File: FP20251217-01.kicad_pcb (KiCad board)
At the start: 2 copper layers, 1 part, among them J1 216-3340-00-0602J

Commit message: Roughing out PCB
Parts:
- added A1: Arduino_UNO_R2, Module:Arduino_UNO_R2, F.Cu at (150.0, 100.0)
- added C1: 0.1u, Capacitor_THT:C_Disc_D4.7mm_W2.5mm_P5.00mm, F.Cu at (129.2, 97.7)
- added J6: Display, Connector_PinSocket_2.54mm:PinSocket_1x04_P2.54mm_Vertical, F.Cu at (143.4, 88.5)
- added J7: Read Button, Connector_PinSocket_2.54mm:PinSocket_1x02_P2.54mm_Vertical, F.Cu at (111.0, 89.7)
- added R1: 10k, Resistor_THT:R_Axial_DIN0207_L6.3mm_D2.5mm_P10.16mm_Horizontal, F.Cu at (106.3, 111.0)
- added R10: 10k, Resistor_THT:R_Axial_DIN0207_L6.3mm_D2.5mm_P10.16mm_Horizontal, F.Cu at (146.5, 105.0)
- added R11: 10k, Resistor_THT:R_Axial_DIN0207_L6.3mm_D2.5mm_P10.16mm_Horizontal, F.Cu at (116.2, 103.2)
- added R2: 10k, Resistor_THT:R_Axial_DIN0207_L6.3mm_D2.5mm_P10.16mm_Horizontal, F.Cu at (106.3, 113.5)
- added R3: 10k, Resistor_THT:R_Axial_DIN0207_L6.3mm_D2.5mm_P10.16mm_Horizontal, F.Cu at (106.3, 117.5)
- added R4: 10k, Resistor_THT:R_Axial_DIN0207_L6.3mm_D2.5mm_P10.16mm_Horizontal, F.Cu at (106.3, 120.1)
- added R5: 10k, Resistor_THT:R_Axial_DIN0207_L6.3mm_D2.5mm_P10.16mm_Horizontal, F.Cu at (106.3, 122.6)
- added R6: 10k, Resistor_THT:R_Axial_DIN0207_L6.3mm_D2.5mm_P10.16mm_Horizontal, F.Cu at (106.3, 125.2)
- added R7: 10k, Resistor_THT:R_Axial_DIN0207_L6.3mm_D2.5mm_P10.16mm_Horizontal, F.Cu at (106.3, 127.7)
- added R8: 10k, Resistor_THT:R_Axial_DIN0207_L6.3mm_D2.5mm_P10.16mm_Horizontal, F.Cu at (106.3, 130.2)
- added R9: 10k, Resistor_THT:R_Axial_DIN0207_L6.3mm_D2.5mm_P10.16mm_Horizontal, F.Cu at (146.5, 107.5)
- moved J1 43.6 mm to (123.1, 112.3)
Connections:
- J1 pad 1: unconnected-(J1-Pad1) -> /O1
- J1 pad 10: unconnected-(J1-Pad10) -> /A0
- J1 pad 11: unconnected-(J1-Pad11) -> /A1
- J1 pad 12: unconnected-(J1-Pad12) -> /A2
- J1 pad 13: unconnected-(J1-Pad13) -> /A3
- J1 pad 14: unconnected-(J1-Pad14) -> /A4
- J1 pad 15: unconnected-(J1-Pad15) -> /~{CE}
- J1 pad 16: unconnected-(J1-Pad16) -> +5V
- J1 pad 2: unconnected-(J1-Pad2) -> /O2
- J1 pad 3: unconnected-(J1-Pad3) -> /O3
- J1 pad 4: unconnected-(J1-Pad4) -> /O4
- J1 pad 5: unconnected-(J1-Pad5) -> /O5
- J1 pad 6: unconnected-(J1-Pad6) -> /O6
- J1 pad 7: unconnected-(J1-Pad7) -> /O7
- J1 pad 8: unconnected-(J1-Pad8) -> GND
- J1 pad 9: unconnected-(J1-Pad9) -> /O8
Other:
- board outline added: 53.6 x 55.6 mm

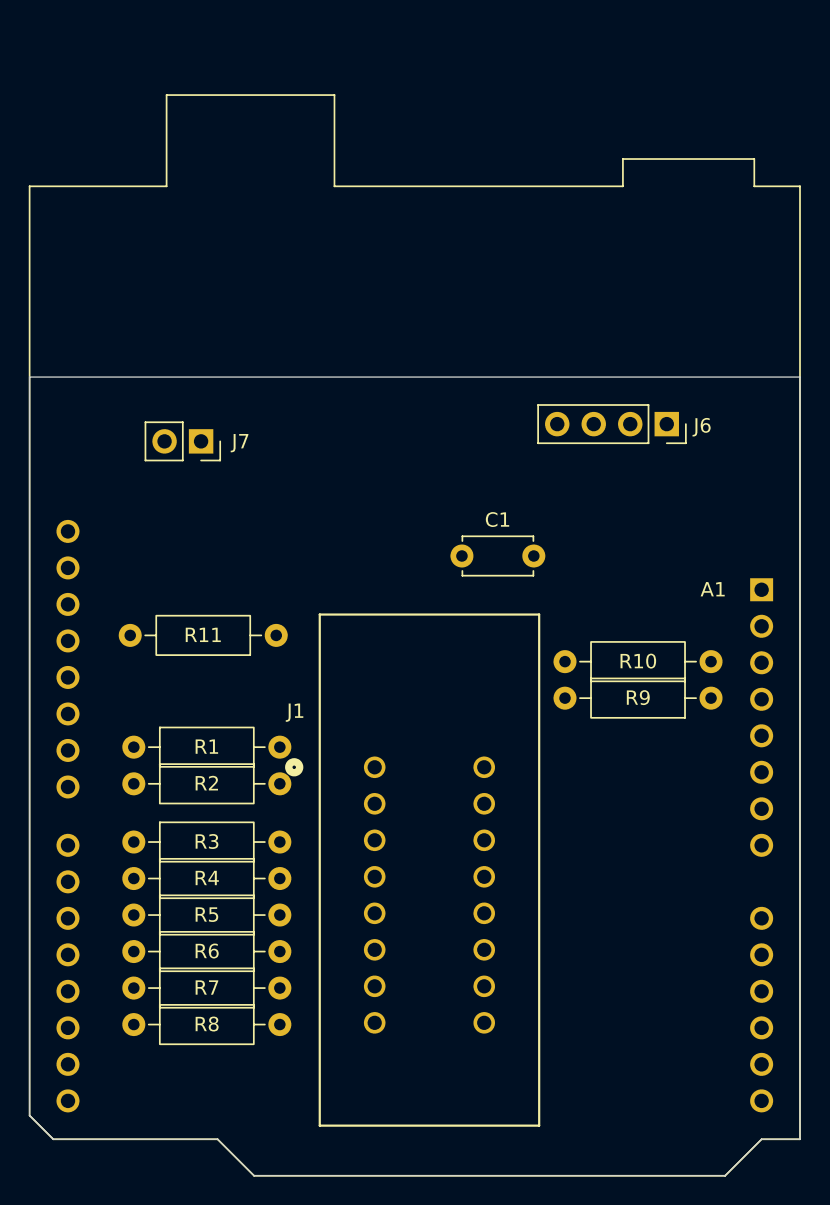
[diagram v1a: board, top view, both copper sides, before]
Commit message: Added planes
Since holes will not inherently be plated through holes, I tried to maintain connection to components entirely on one side. A few traces are on the top side, with the intention of them be soldered from above in addition to below. I also placed a few large vias, with the idea being the solder will join them together. Can't wait to get my CNC machine and try this out!
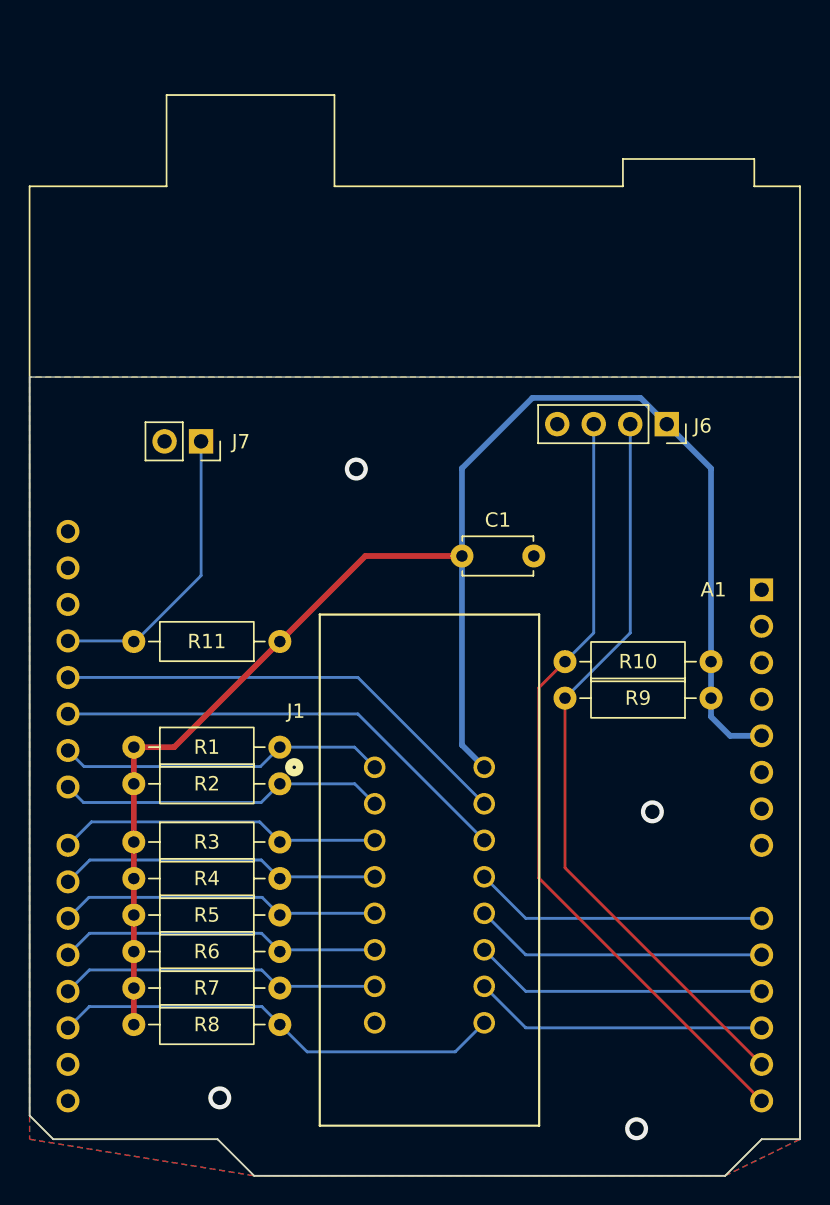
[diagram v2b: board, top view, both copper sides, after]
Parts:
- moved R11 0.49 mm to (116.5, 103.6)
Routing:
- net +5V: track 0.00 -> 111.8 mm
- net /SCL: track 0.00 -> 55.1 mm
- net /SDA: track 0.00 -> 52.1 mm
- net /~{CE}: track 0.00 -> 32.6 mm
- net /A4: track 0.00 -> 32.6 mm
- net /O8: track 0.00 -> 31.7 mm
- net /O1: track 0.00 -> 22.9 mm
- net /O2: track 0.00 -> 22.9 mm
- net /O3: track 0.00 -> 22.6 mm
- net /O4: track 0.00 -> 22.6 mm
- net /O6: track 0.00 -> 22.5 mm
- net /O7: track 0.00 -> 22.5 mm
- net /O5: track 0.00 -> 22.5 mm
- net /A3: track 0.00 -> 20.5 mm
- net /A2: track 0.00 -> 20.5 mm
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- added copper zone on B.Cu, net GND
- added copper zone on F.Cu, net GND
